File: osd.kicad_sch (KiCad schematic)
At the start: 9 parts, among them U35 STM32G431KBUx

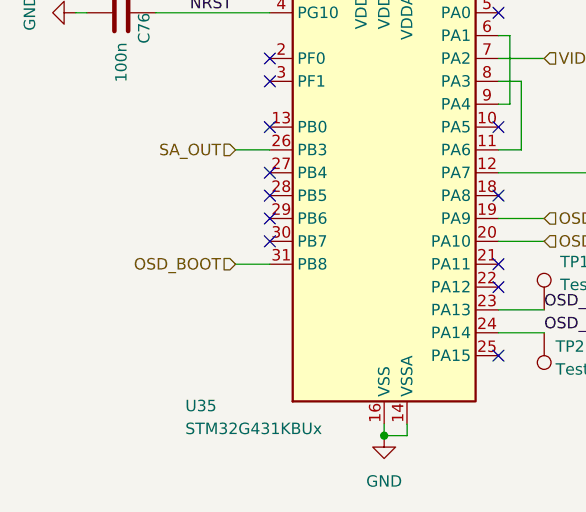
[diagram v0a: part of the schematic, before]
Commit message: Added Open-OSD-X and new layout
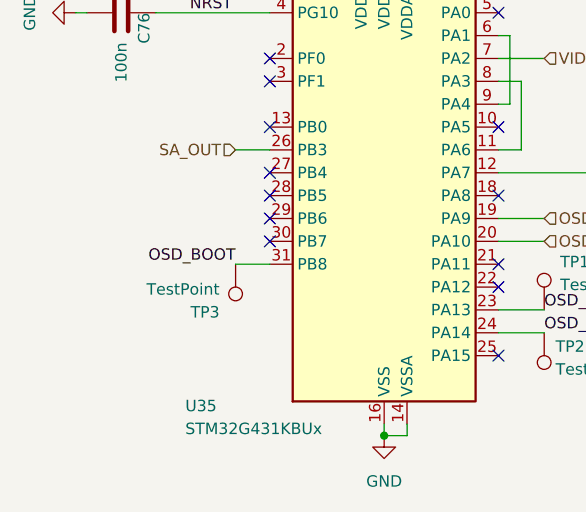
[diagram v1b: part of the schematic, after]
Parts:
- added TP3: TestPoint, TestPoint:TestPoint_Pad_D1.0mm, symbol Connector:TestPoint
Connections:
- net OSD_BOOT: now also TP3.1
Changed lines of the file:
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@@
+		)
+	)
+	(label "OSD_BOOT"
+		(at 130.81 116.84 180)
+		(effects
+			(font
+				(size 1.27 1.27)
+			)
+			(justify right bottom)
 		)
 	)
@@
 		)
 	)
-	(hierarchical_label "OSD_BOOT"
-		(shape input)
-		(at 130.81 116.84 180)
-		(effects
-			(font
-				(size 1.27 1.27)
-			)
-			(justify right)
-		)
-	)
 	(hierarchical_label "OSD_TX"
 		(shape input)
@@
 		)
 		(instances
-			(project ""
+			(project "OpenFC"
 				(path "/fb88b6f9-ee39-4640-a9d4-04a17ceeac64/cd9508c6-33b2-4092-8e87-ecfbafcee27b"
 					(reference "L1")
@@
 	(symbol
 		(lib_id "Connector:TestPoint")
+		(at 130.81 116.84 180)
+		(unit 1)
+		(exclude_from_sim no)
+		(in_bom yes)
+		(on_board yes)
+		(dnp no)
+		(property "Reference" "TP3"
+			(at 129.032 122.174 0)
+			(effects
+				(font
+					(size 1.27 1.27)
+				)
+				(justify left)
+			)
+		)
+		(property "Value" "TestPoint"
+			(at 129.032 119.634 0)
+			(effects
+				(font
+					(size 1.27 1.27)
+				)
+				(justify left)
+			)
+		)
+		(property "Footprint" "TestPoint:TestPoint_Pad_D1.0mm"
+			(at 125.73 116.84 0)
+			(effects
+				(font
+					(size 1.27 1.27)
+				)
+				(hide yes)
+			)
+		)
+		(property "Datasheet" "~"
+			(at 125.73 116.84 0)
+			(effects
+				(font
+					(size 1.27 1.27)
+				)
+				(hide yes)
+			)
+		)
+		(property "Description" "test point"
+			(at 130.81 116.84 0)
+			(effects
+				(font
+					(size 1.27 1.27)
+				)
+				(hide yes)
+			)
+		)
+		(pin "1"
+		)
+		(instances
+			(project "OpenFC"
+				(path "/fb88b6f9-ee39-4640-a9d4-04a17ceeac64/cd9508c6-33b2-4092-8e87-ecfbafcee27b"
+					(reference "TP3")
+					(unit 1)
+				)
+			)
+		)
+	)
+	(symbol
+		(lib_id "Connector:TestPoint")
 		(at 165.1 121.92 0)
 		(unit 1)
@@
 		)
 		(instances
-			(project ""
+			(project "OpenFC"
 				(path "/fb88b6f9-ee39-4640-a9d4-04a17ceeac64/cd9508c6-33b2-4092-8e87-ecfbafcee27b"
 					(reference "TP1")

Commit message: Ordered first revision
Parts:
- added C49: 100n, Capacitor_SMD:C_0402_1005Metric, symbol Device:C
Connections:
- net +3.3V: now also C49.1
- net GND: now also C49.2
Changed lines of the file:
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@@
-	(wire
-		(pts
-			(xy 160.02 93.98) (xy 165.1 93.98)
-		)
-		(stroke
-			(width 0)
-			(type default)
-		)
-	)
 	(wire
 		(pts
@@
 	(wire
 		(pts
+			(xy 121.92 59.69) (xy 121.92 64.77)
+		)
+		(stroke
+			(width 0)
+			(type default)
+		)
+	)
+	(wire
+		(pts
 			(xy 176.53 77.47) (xy 176.53 80.01)
 		)
@@
 	(wire
 		(pts
+			(xy 121.92 48.26) (xy 121.92 52.07)
+		)
+		(stroke
+			(width 0)
+			(type default)
+		)
+	)
+	(wire
+		(pts
 			(xy 149.86 66.04) (xy 149.86 83.82)
 		)
@@
 		(pts
 			(xy 147.32 81.28) (xy 144.78 81.28)
+		)
+		(stroke
+			(width 0)
+			(type default)
+		)
+	)
+	(wire
+		(pts
+			(xy 160.02 93.98) (xy 184.15 93.98)
 		)
 		(stroke
@@
 	(hierarchical_label "VIDEO_OUT"
 		(shape input)
-		(at 165.1 93.98 0)
+		(at 184.15 93.98 0)
 		(effects
 			(font
@@
 	)
 	(symbol
+		(lib_id "power:+3.3V")
+		(at 121.92 48.26 0)
+		(unit 1)
+		(exclude_from_sim no)
+		(in_bom yes)
+		(on_board yes)
+		(dnp no)
+		(fields_autoplaced yes)
+		(property "Reference" "#PWR0104"
+			(at 121.92 52.07 0)
+			(effects
+				(font
+					(size 1.27 1.27)
+				)
+				(hide yes)
+			)
+		)
+		(property "Value" "+3.3V"
+			(at 121.92 43.18 0)
+			(effects
+				(font
+					(size 1.27 1.27)
+				)
+			)
+		)
+		(property "Footprint" ""
+			(at 121.92 48.26 0)
+			(effects
+				(font
+					(size 1.27 1.27)
+				)
+				(hide yes)
+			)
+		)
+		(property "Datasheet" ""
+			(at 121.92 48.26 0)
+			(effects
+				(font
+					(size 1.27 1.27)
+				)
+				(hide yes)
+			)
+		)
+		(property "Description" "Power symbol creates a global label with name \"+3.3V\""
+			(at 121.92 48.26 0)
+			(effects
+				(font
+					(size 1.27 1.27)
+				)
+				(hide yes)
+			)
+		)
+		(pin "1"
+		)
+		(instances
+			(project "OpenFC"
+				(path "/fb88b6f9-ee39-4640-a9d4-04a17ceeac64/cd9508c6-33b2-4092-8e87-ecfbafcee27b"
+					(reference "#PWR0104")
+					(unit 1)
+				)
+			)
+		)
+	)
+	(symbol
+		(lib_id "power:GND")
+		(at 121.92 64.77 0)
+		(unit 1)
+		(exclude_from_sim no)
+		(in_bom yes)
+		(on_board yes)
+		(dnp no)
+		(fields_autoplaced yes)
+		(property "Reference" "#PWR0129"
+			(at 121.92 71.12 0)
+			(effects
+				(font
+					(size 1.27 1.27)
+				)
+				(hide yes)
+			)
+		)
+		(property "Value" "GND"
+			(at 121.92 69.85 0)
+			(effects
+				(font
+					(size 1.27 1.27)
+				)
+			)
+		)
+		(property "Footprint" ""
+			(at 121.92 64.77 0)
+			(effects
+				(font
+					(size 1.27 1.27)
+				)
+				(hide yes)
+			)
+		)
+		(property "Datasheet" ""
+			(at 121.92 64.77 0)
+			(effects
+				(font
+					(size 1.27 1.27)
+				)
+				(hide yes)
+			)
+		)
+		(property "Description" "Power symbol creates a global label with name \"GND\" , ground"
+			(at 121.92 64.77 0)
+			(effects
+				(font
+					(size 1.27 1.27)
+				)
+				(hide yes)
+			)
+		)
+		(pin "1"
+		)
+		(instances
+			(project "OpenFC"
+				(path "/fb88b6f9-ee39-4640-a9d4-04a17ceeac64/cd9508c6-33b2-4092-8e87-ecfbafcee27b"
+					(reference "#PWR0129")
+					(unit 1)
+				)
+			)
+		)
+	)
+	(symbol
 		(lib_id "lib:BLM15AG601SN1D")
 		(at 149.86 58.42 270)
@@
 					(unit 1)
 				)
+			)
+		)
+	)
+	(symbol
+		(lib_id "Device:C")
+		(at 121.92 55.88 0)
+		(unit 1)
+		(exclude_from_sim no)
+		(in_bom yes)
+		(on_board yes)
+		(dnp no)
+		(property "Reference" "C49"
+			(at 121.92 53.34 0)
+			(effects
+				(font
+					(size 1.27 1.27)
+				)
+				(justify left)
+			)
+		)
+		(property "Value" "100n"
+			(at 125.222 55.88 0)
+			(effects
+				(font
+					(size 1.27 1.27)
+				)
+				(justify left)
+			)
+		)
+		(property "Footprint" "Capacitor_SMD:C_0402_1005Metric"
+			(at 122.8852 59.69 0)
+			(effects
+				(font
+					(size 1.27 1.27)
+				)
+				(hide yes)
+			)
+		)
+		(property "Datasheet" "~"
+			(at 121.92 55.88 0)
+			(effects
+				(font
+					(size 1.27 1.27)
+				)
+				(hide yes)
+			)
+		)
+		(property "Description" ""
+			(at 121.92 55.88 0)
+			(effects
+				(font
+					(size 1.27 1.27)
+				)
+			)
+		)
+		(property "LCSC" "C1525"
+			(at 121.92 55.88 0)
+			(effects
+				(font
+					(size 1.27 1.27)
+				)
+				(hide yes)
+			)
+		)
+		(pin "1"
+		)
+		(pin "2"
+		)
+		(instances
+			(project "OpenFC"
+				(path "/fb88b6f9-ee39-4640-a9d4-04a17ceeac64/cd9508c6-33b2-4092-8e87-ecfbafcee27b"
+					(reference "C49")
+					(unit 1)
+				)

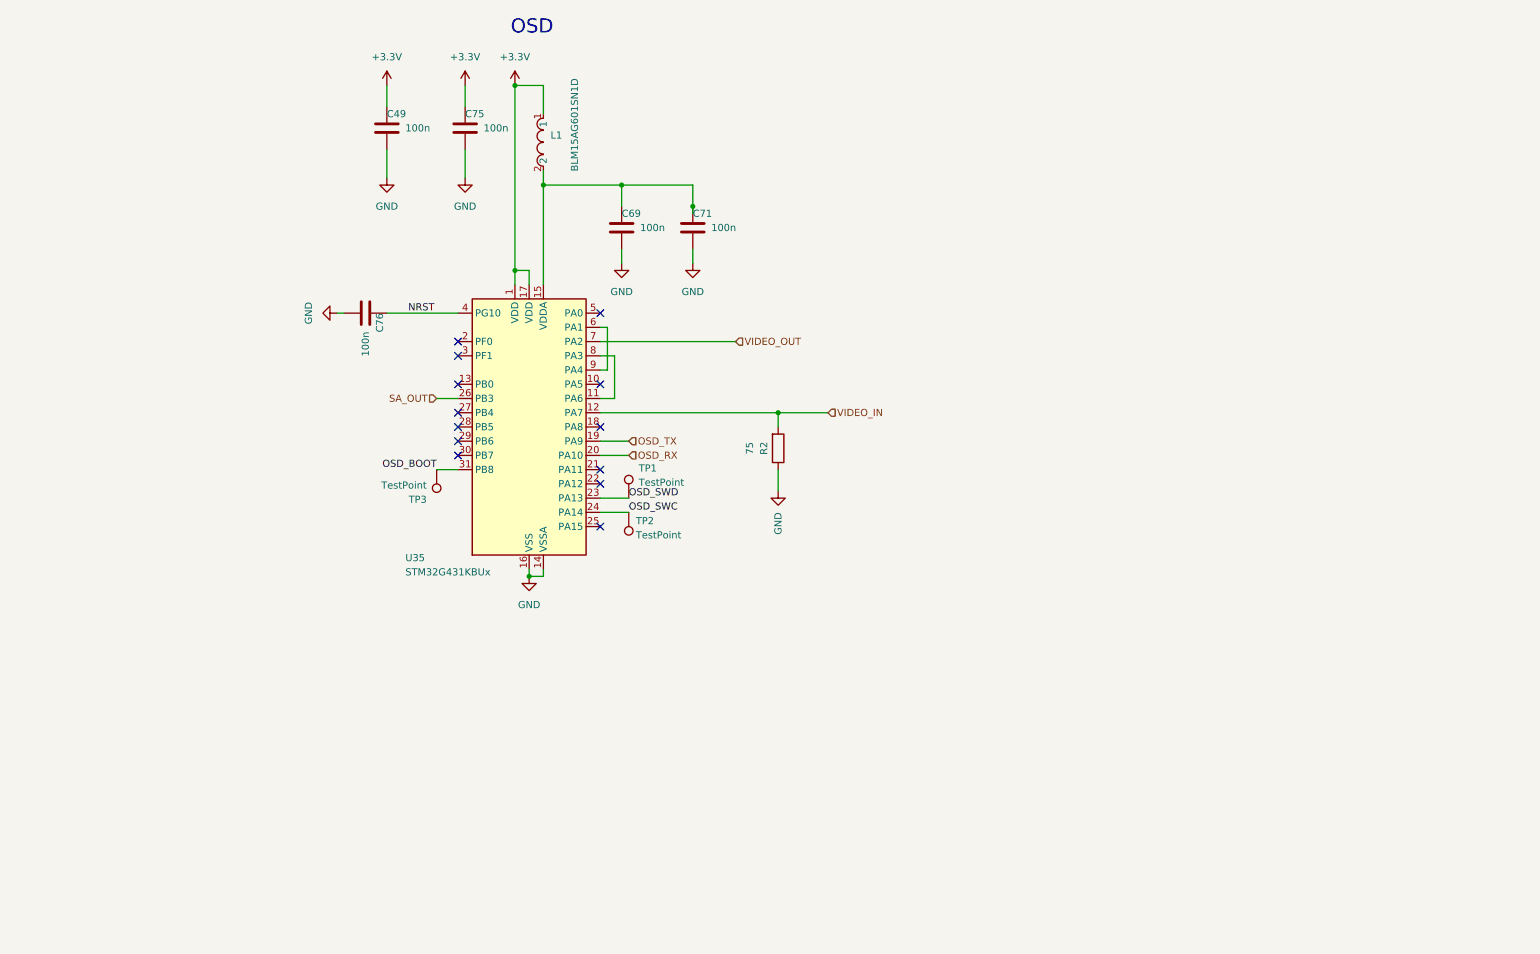
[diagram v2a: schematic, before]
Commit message: Switched to RP2354B for V2 of the FC for more IO. I want to try implement OSD on PIO state machine. I know BF already uses all of them but it should be possible and then later try to combine it witht the WS2812 protocol PIO2. If anybody here has any experience with analog OSD generation let me know, I just want to make a circuit that would allow further software development later. The reason I want to do it this way is it's cheap BOM<1 euro and low footprint, just 2 2x2 IC's and some passives.
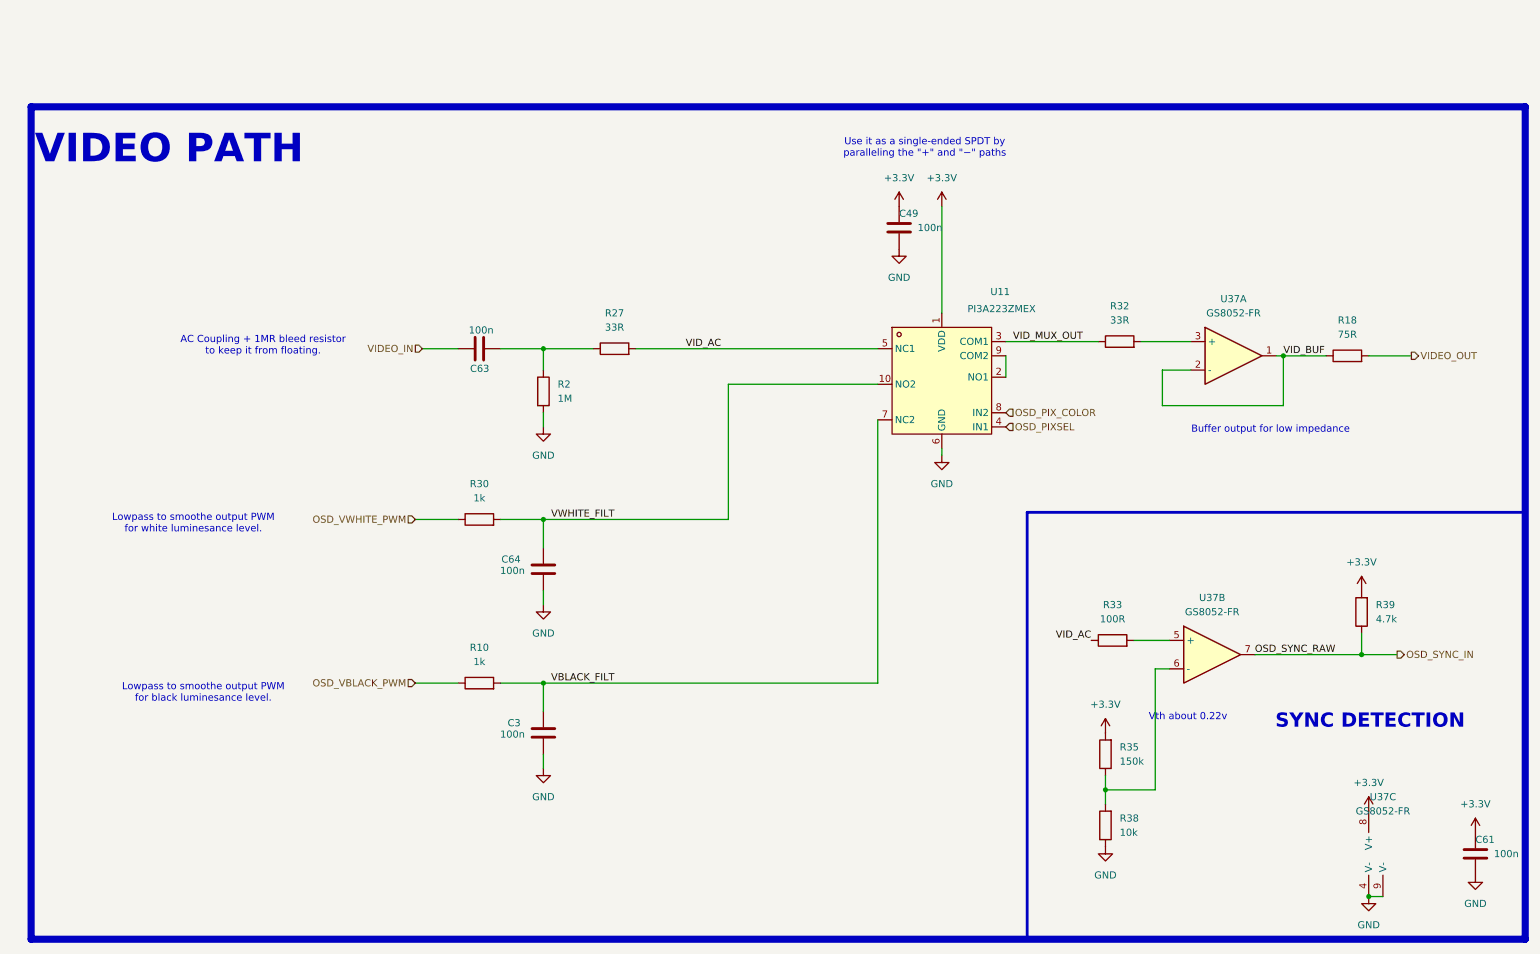
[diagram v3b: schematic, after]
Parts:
- removed C69, C71, C75, C76: 100n, Capacitor_SMD:C_0402_1005Metric, symbol Device:C
- removed L1: BLM15AG601SN1D, lib:L0402, symbol lib:BLM15AG601SN1D
- removed TP1, TP2, TP3: TestPoint, TestPoint:TestPoint_Pad_D1.0mm, symbol Connector:TestPoint
- removed U35: STM32G431KBUx, Package_DFN_QFN:QFN-32-1EP_5x5mm_P0.5mm_EP3.1x3.1mm, symbol MCU_ST_STM32G4:STM32G431KBUx
- added C3, C61, C63, C64: 100n, Capacitor_SMD:C_0402_1005Metric, symbol Device:C
- added R10, R30: 1k, Resistor_SMD:R_0402_1005Metric, symbol Device:R
- added R18: 75R, Resistor_SMD:R_0402_1005Metric, symbol Device:R
- added R27, R32: 33R, Resistor_SMD:R_0402_1005Metric, symbol Device:R
- added R33: 100R, Resistor_SMD:R_0402_1005Metric, symbol Device:R
- added R35: 150k, Resistor_SMD:R_0402_1005Metric, symbol Device:R
- added R38: 10k, Resistor_SMD:R_0402_1005Metric, symbol Device:R
- added R39: 4.7k, Resistor_SMD:R_0402_1005Metric, symbol Device:R
- added U11: PI3A223ZMEX, lib:UQFN-10_L1.8-W1.4-P0.40-TL, symbol lib:PI3A223ZMEX
- added U37: GS8052-FR, Package_SON:WSON-8-1EP_2x2mm_P0.5mm_EP0.9x1.6mm, symbol Device:Opamp_Dual
- R2: value 75 -> 1M; LCSC C11702 -> (none)
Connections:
- net +3.3V: now also C61.1, R35.2, R39.2, U11.1 (VDD), U37.8 (V+)
- net GND: now also R2.2, C3.1, C61.2, C64.1, R38.1, U11.6 (GND), U37.4 (V-), U37.9 (V-); no longer R2.1
- net VIDEO_IN: now also C63.1; no longer R2.2
- net VIDEO_OUT: now also R18.2
- new net: C63.2, R2.1, R27.1
- new net: R32.2, U37.3 (+)
- new net: R35.1, R38.2, U37.6 (-)
- new net: U11.2 (NO1), U11.9 (COM2)
- new net: R33.2, U37.5 (+)
- new net OSD_PIXSEL: U11.4 (IN1)
- new net OSD_PIX_COLOR: U11.8 (IN2)
- new net OSD_SYNC_IN: R39.1, U37.7
- new net OSD_VBLACK_PWM: R10.1
- new net OSD_VWHITE_PWM: R30.1
- new net VBLACK_FILT: C3.2, R10.2, U11.7 (NC2)
- new net VID_AC: R27.2, R33.1, U11.5 (NC1)
- new net VID_BUF: R18.1, U37.1, U37.2 (-)
- new net VID_MUX_OUT: R32.1, U11.3 (COM1)
- new net VWHITE_FILT: C64.2, R30.2, U11.10 (NO2)
- no-connect marks 13 -> 0
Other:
- note added: "AC Coupling + 1MR bleed resistor to keep it from floating."
- note added: "Buffer output for low impedance"
- note added: "Lowpass to smoothe output PWM for black luminesance level."
- note added: "Lowpass to smoothe output PWM for white luminesance level."
- note added: "SYNC DETECTION"
- note added: "Use it as a single-ended SPDT by paralleling the "+" and "−" paths"
- note added: "VIDEO PATH"
- note added: "Vth about 0.22v"
- note removed: "OSD"
